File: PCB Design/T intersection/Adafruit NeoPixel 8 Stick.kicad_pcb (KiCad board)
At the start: 2 copper layers, 36.2 x 28.6 mm, 8 parts, among them CN1 1X4SMT, CN2 1X4SMT, CN3 1X4SMT

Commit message: changes to T intersection
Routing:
- net GND: track 28.2 -> 0.00 mm, vias 3 -> 0
- net Net-(CN1-Pad2): track 14.4 -> 12.1 mm
- net Net-(CN2-Pad3): track 0.00 -> 2.23 mm
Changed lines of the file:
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@@
   (segment (start 146.210959 99.244218) (end 147.382211 99.244218) (width 0.25) (layer "F.Cu") (net 1))
   (segment (start 133.274 109.55) (end 137.483782 105.340218) (width 0.25) (layer "F.Cu") (net 1))
-  (segment (start 128.942 109.818) (end 128.942 109.55) (width 0.25) (layer "F.Cu") (net 1))
   (segment (start 128.942 109.55) (end 133.274 109.55) (width 0.25) (layer "F.Cu") (net 1))
   (segment (start 137.483782 105.340218) (end 137.483782 101.506959) (width 0.25) (layer "F.Cu") (net 1))
   (segment (start 126.238 112.522) (end 128.942 109.818) (width 0.25) (layer "F.Cu") (net 1))
+  (segment (start 146.210959 99.244218) (end 144.964218 99.244218) (width 0.25) (layer "F.Cu") (net 1))
+  (segment (start 144.964218 99.244218) (end 144.78 99.06) (width 0.25) (layer "F.Cu") (net 1))
   (segment (start 147.382211 99.244218) (end 152.49 104.352007) (width 0.25) (layer "F.Cu") (net 1))
   (via (at 152.4 106.426) (size 0.8) (drill 0.4) (layers "F.Cu" "B.Cu") (net 1))
   (via (at 126.238 112.522) (size 0.8) (drill 0.4) (layers "F.Cu" "B.Cu") (net 1))
   (via (at 144.773 93.987) (size 0.8) (drill 0.4) (layers "F.Cu" "B.Cu") (net 1))
-  (segment (start 155.194 112.776) (end 154.044 112.776) (width 0.25) (layer "B.Cu") (net 1))
   (segment (start 152.4 111.132) (end 152.4 106.426) (width 0.25) (layer "B.Cu") (net 1))
   (segment (start 154.044 112.776) (end 152.4 111.132) (width 0.25) (layer "B.Cu") (net 1))
-  (segment (start 126.238 105.41) (end 126.238 106.426) (width 0.25) (layer "F.Cu") (net 2))
-  (segment (start 139.116 94.412) (end 138.938 94.234) (width 0.25) (layer "F.Cu") (net 2))
-  (segment (start 125.61 104.782) (end 126.238 105.41) (width 0.25) (layer "F.Cu") (net 2))
-  (segment (start 139.116 96.43) (end 139.116 94.412) (width 0.25) (layer "F.Cu") (net 2))
-  (segment (start 131.756218 102.709041) (end 127.682959 102.709041) (width 0.25) (layer "F.Cu") (net 2))
-  (segment (start 125.61 104.782) (end 124.042 106.35) (width 0.25) (layer "F.Cu") (net 2))
-  (segment (start 127.682959 102.709041) (end 125.61 104.782) (width 0.25) (layer "F.Cu") (net 2))
-  (via (at 147.32 104.902) (size 0.8) (drill 0.4) (layers "F.Cu" "B.Cu") (net 2))
-  (via (at 126.238 106.426) (size 0.8) (drill 0.4) (layers "F.Cu" "B.Cu") (net 2))
-  (via (at 138.938 94.234) (size 0.8) (drill 0.4) (layers "F.Cu" "B.Cu") (net 2))
-  (segment (start 147.32 109.052) (end 147.32 104.902) (width 0.25) (layer "B.Cu") (net 2))
-  (segment (start 154.044 115.776) (end 147.32 109.052) (width 0.25) (layer "B.Cu") (net 2))
-  (segment (start 155.194 115.776) (end 154.044 115.776) (width 0.25) (layer "B.Cu") (net 2))
-  (segment (start 135.962 94.868) (end 135.962 93.725998) (width 0.25) (layer "B.Cu") (net 3))
   (segment (start 127.388 103.442) (end 135.962 94.868) (width 0.25) (layer "B.Cu") (net 3))
-  (segment (start 126.238 103.442) (end 127.388 103.442) (width 0.25) (layer "B.Cu") (net 3))
-  (via (at 124.206 109.728) (size 0.8) (drill 0.4) (layers "F.Cu" "B.Cu") (net 4))
+  (segment (start 126.162 109.55) (end 126.238 109.474) (width 0.25) (layer "F.Cu") (net 4))
+  (segment (start 124.042 109.55) (end 126.162 109.55) (width 0.25) (layer "F.Cu") (net 4))
+  (via (at 126.238 109.474) (size 0.8) (drill 0.4) (layers "F.Cu" "B.Cu") (net 4))
   (segment (start 128.942 106.35) (end 132.640741 106.35) (width 0.25) (layer "F.Cu") (net 5))
   (segment (start 132.640741 106.35) (end 134.018959 104.971782) (width 0.25) (layer "F.Cu") (net 5))
@@
   (segment (start 135.221041 95.424959) (end 139.116 91.53) (width 0.25) (layer "F.Cu") (net 6))
   (segment (start 126.245998 100.442) (end 132.962 93.725998) (width 0.25) (layer "B.Cu") (net 7))
-  (segment (start 126.238 100.442) (end 126.245998 100.442) (width 0.25) (layer "B.Cu") (net 7))
-  (segment (start 142.24 96.354) (end 142.316 96.43) (width 0.25) (layer "F.Cu") (net 8))
   (segment (start 142.24 94.234) (end 142.24 96.354) (width 0.25) (layer "F.Cu") (net 8))
   (via (at 142.24 94.234) (size 0.8) (drill 0.4) (layers "F.Cu" "B.Cu") (net 8))
@@
     (polygon
       (pts
-        (xy 184.5945 133.096)
-        (xy 115.3287 133.096)
-        (xy 115.3287 87.0712)
-        (xy 184.5945 87.0712)
+        (xy 164.338 86.36)
+        (xy 163.83 124.206)
+        (xy 118.872 123.444)
+        (xy 118.618 86.614)
       )
     )

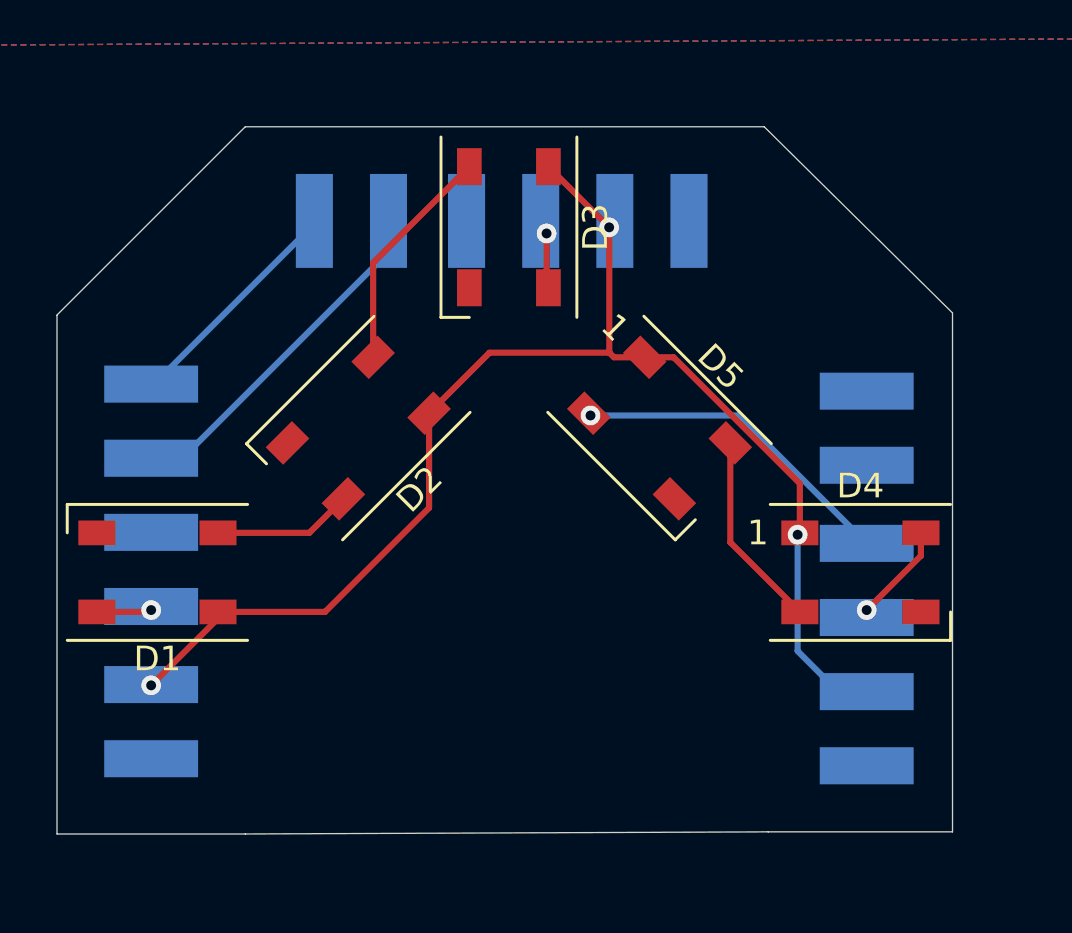
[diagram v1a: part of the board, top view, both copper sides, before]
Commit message: left t junction update
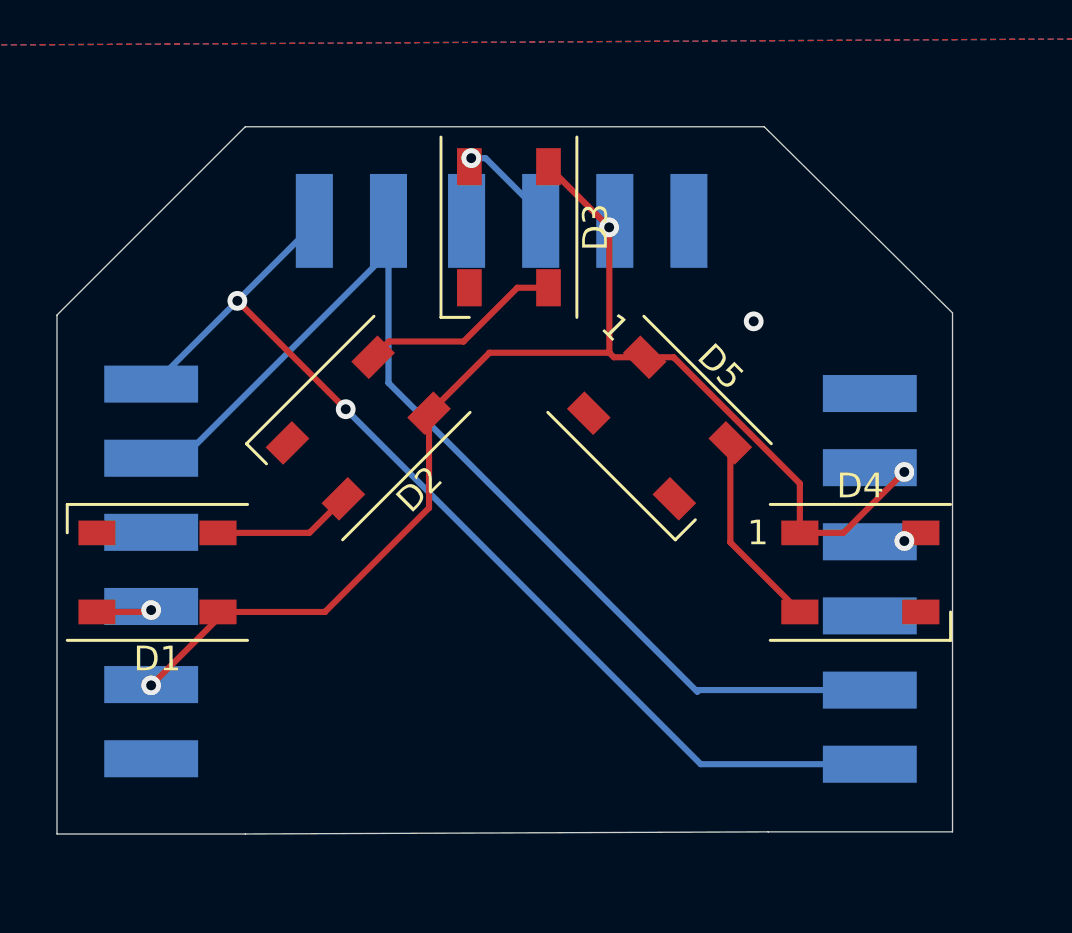
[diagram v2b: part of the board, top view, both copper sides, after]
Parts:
- moved CN3 1.14 mm to (154.7, 108.7)
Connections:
- CN3 pad 1: unconnected-(CN3-Pad1) -> GND
- CN3 pad 2: unconnected-(CN3-Pad2) -> +5V
- CN3 pad 4: Net-(CN3-Pad4) -> GND
- CN3 pad 5: +5V -> Net-(CN1-Pad2)
- CN3 pad 6: GND -> Net-(CN1-Pad1)
- D3 pad 2: Net-(D2-Pad2) -> Net-(CN1-Pad4)
- D3 pad 4: Net-(CN1-Pad4) -> Net-(D2-Pad2)
- D4 pad 4: Net-(CN3-Pad4) -> Net-(CN3-Pad3)
- D5 pad 2: Net-(CN3-Pad3) -> unconnected-(D5-Pad2)
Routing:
- net Net-(CN1-Pad1): track 9.50 -> 42.9 mm, vias 0 -> 2
- net Net-(CN1-Pad2): track 12.1 -> 43.4 mm
- net Net-(CN3-Pad3): track 13.3 -> 0.00 mm
- net Net-(CN3-Pad4): track 4.03 -> 0.00 mm, vias 1 -> 0
- net Net-(CN1-Pad4): track 2.12 -> 4.04 mm
- net +5V: track 53.7 -> 52.0 mm
- net Net-(D2-Pad2): track 9.33 -> 8.26 mm
- net GND: vias 0 -> 1
